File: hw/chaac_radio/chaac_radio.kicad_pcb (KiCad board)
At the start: 4 copper layers, 40 x 20 mm, 22 parts, among them J1 20021321-00016C4LF, J2 20021321-00016C4LF, J3 TC2030-CTX, J4 RP_SMA, U3 NRF52811-QFAA, Y1 32.768kHz, Y2 32MHz

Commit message: Progress with chaac base
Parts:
- moved J4 63.6 mm to (162.4, 100.0)
- moved C14 63.2 mm to (144.0, 97.0)
- moved C16 63.2 mm to (152.6, 93.0)
- moved C17 63.2 mm to (153.6, 93.0)
- moved U3 63.2 mm to (148.7, 99.8)
- moved Y1 63.2 mm to (141.7, 103.7)
- moved C10 63.2 mm to (143.6, 103.0)
- moved C11 63.2 mm to (140.8, 100.9)
- moved C13 63.2 mm to (149.1, 105.4)
- moved C15 63.2 mm to (146.5, 93.0)
- moved C18 63.2 mm to (151.6, 93.0)
- moved C19 63.2 mm to (147.5, 93.0)
- moved F1 63.2 mm to (152.5, 96.4)
- moved J1 63.2 mm to (135.0, 100.0)
- moved J2 63.2 mm to (158.0, 100.0)
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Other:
- outline, holes or cut-outs redrawn

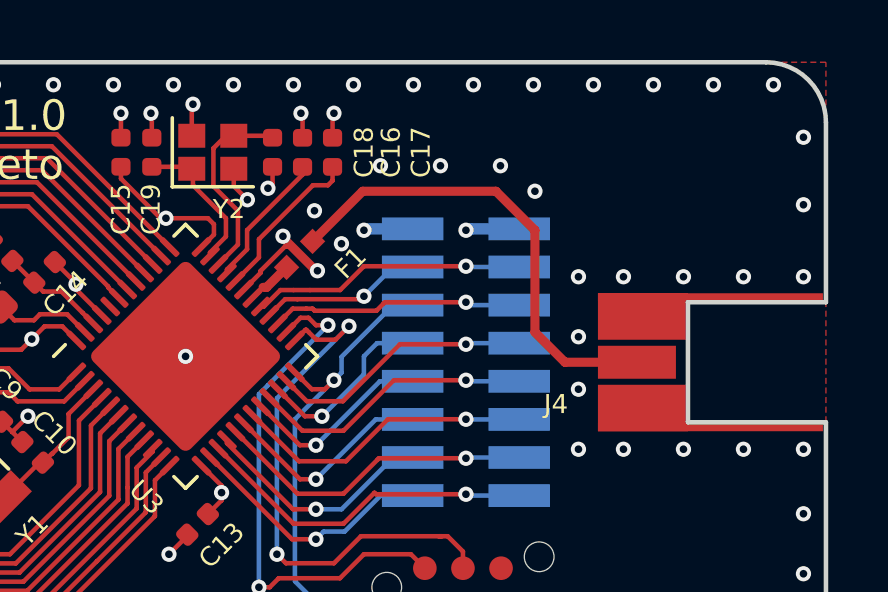
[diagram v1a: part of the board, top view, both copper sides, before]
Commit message: Updated bom and matched trace for JLCPCB impedance control
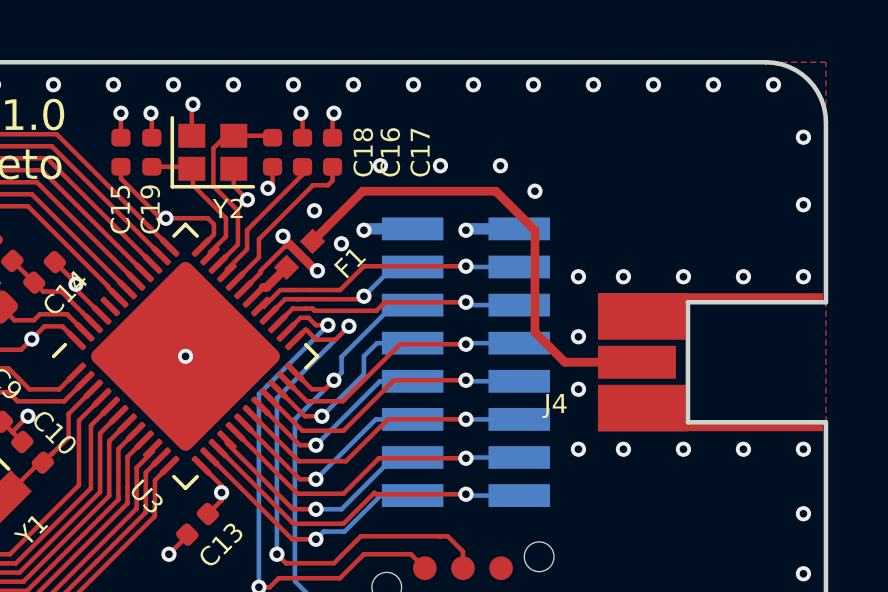
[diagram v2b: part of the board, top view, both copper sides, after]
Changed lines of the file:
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@@
   )
   (setup
-    (last_trace_width 0.3048)
+    (last_trace_width 0.1524)
     (user_trace_width 0.127)
     (user_trace_width 0.1524)
@@
   (segment (start 149.749785 96.727483) (end 150.4 96.077268) (width 0.1524) (layer F.Cu) (net 7))
   (segment (start 150.4 96.077268) (end 150.4 94.95) (width 0.1524) (layer F.Cu) (net 7))
-  (segment (start 151.236612 97.503397) (end 151.35377 97.503397) (width 0.3048) (layer F.Cu) (net 8))
-  (segment (start 151.35377 97.503397) (end 152.020667 96.8365) (width 0.3048) (layer F.Cu) (net 8))
+  (segment (start 151.236612 97.503397) (end 151.35377 97.503397) (width 0.29337) (layer F.Cu) (net 8))
+  (segment (start 151.35377 97.503397) (end 152.020667 96.8365) (width 0.29337) (layer F.Cu) (net 8))
   (segment (start 150.881156 97.858853) (end 151.236612 97.503397) (width 0.1524) (layer F.Cu) (net 8))
   (segment (start 141.396923 96.733328) (end 142.194101 95.93615) (width 0.1524) (layer F.Cu) (net 9))
@@
   (segment (start 150 95.2) (end 148.9 94.1) (width 0.1524) (layer F.Cu) (net 16))
   (segment (start 149.466942 96.34368) (end 150 95.810622) (width 0.1524) (layer F.Cu) (net 16))
-  (segment (start 160.3 95.6) (end 159 94.3) (width 0.3048) (layer F.Cu) (net 17))
-  (segment (start 160.3 99) (end 160.3 95.6) (width 0.3048) (layer F.Cu) (net 17))
-  (segment (start 154.557167 94.3) (end 152.886873 95.970294) (width 0.3048) (layer F.Cu) (net 17))
-  (segment (start 159 94.3) (end 154.557167 94.3) (width 0.3048) (layer F.Cu) (net 17))
-  (segment (start 163.7 100) (end 161.3 100) (width 0.3048) (layer F.Cu) (net 17))
-  (segment (start 161.3 100) (end 160.3 99) (width 0.3048) (layer F.Cu) (net 17))
+  (segment (start 160.3 95.6) (end 159 94.3) (width 0.29337) (layer F.Cu) (net 17))
+  (segment (start 160.3 99) (end 160.3 95.6) (width 0.29337) (layer F.Cu) (net 17))
+  (segment (start 154.557167 94.3) (end 152.886873 95.970294) (width 0.29337) (layer F.Cu) (net 17))
+  (segment (start 159 94.3) (end 154.557167 94.3) (width 0.29337) (layer F.Cu) (net 17))
+  (segment (start 163.7 100) (end 161.3 100) (width 0.29337) (layer F.Cu) (net 17))
+  (segment (start 161.3 100) (end 160.3 99) (width 0.29337) (layer F.Cu) (net 17))
   (via (at 138.8 99.3) (size 0.508) (drill 0.254) (layers F.Cu B.Cu) (net 20))
   (segment (start 136.841 99.3) (end 136.776 99.365) (width 0.1524) (layer B.Cu) (net 20))
